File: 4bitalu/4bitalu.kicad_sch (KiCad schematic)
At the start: 34 parts, among them J1 Power, SW1 Opcode, SW2 Input Value, U1 74LS153 - 0, U2 74LS153 - 1, U3 74LS175, U4 74LS283, U5 74LS00 Stage0-1, U6 74LS00 Stage0-2, U7 74LS00 - Stage1

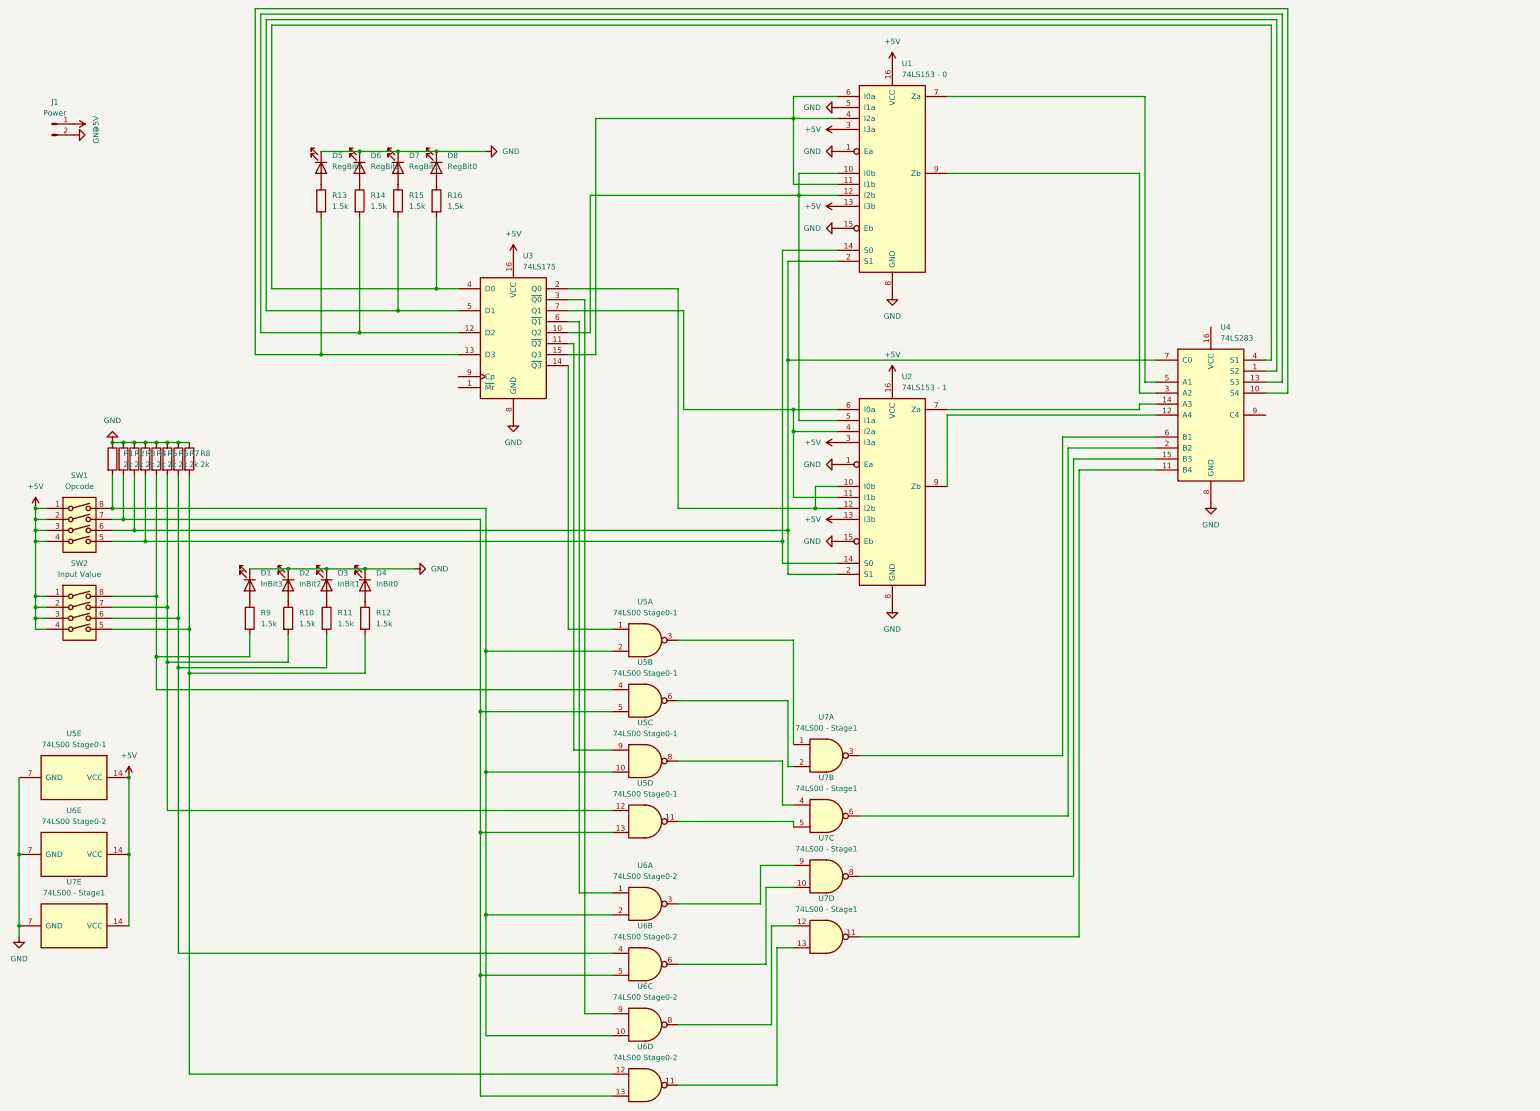
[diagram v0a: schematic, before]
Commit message: Rev 2 of PCB design
Known issues:

 * Pulldown resistors are too high (should be 1k)
 * Missing capacitors for power inputs on chips
 * Inputs on unused NAND gates are not tied high
 * Clock switch is in unexepected orientation
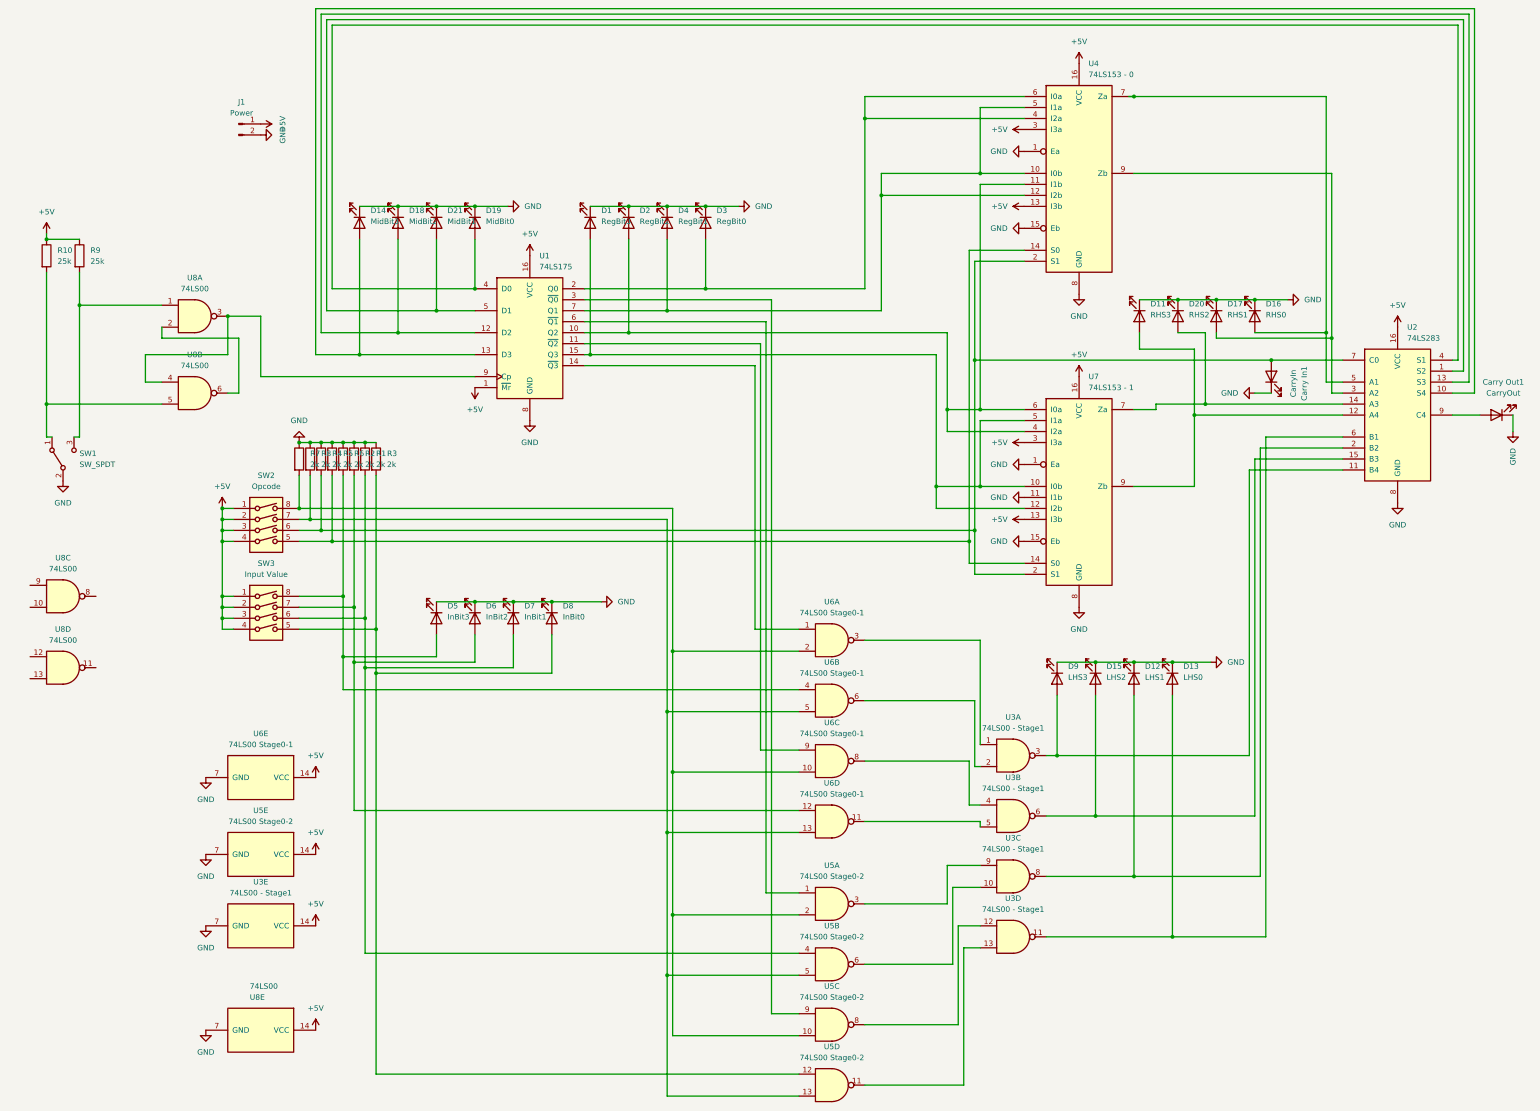
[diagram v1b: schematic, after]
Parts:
- removed R11, R12, R13, R14, R15, R16: 1.5k, Resistor_THT:R_Axial_DIN0204_L3.6mm_D1.6mm_P5.08mm_Horizontal, symbol Device:R
- added Carry In1: CarryIn, LED_THT:LED_D3.0mm, symbol Device:LED
- added Carry Out1: CarryOut, LED_THT:LED_D3.0mm, symbol Device:LED
- added D1: RegBit3, LED_THT:LED_D3.0mm, symbol Device:LED
- added D11: RHS3, LED_THT:LED_D3.0mm, symbol Device:LED
- added D12: LHS1, LED_THT:LED_D3.0mm, symbol Device:LED
- added D13: LHS0, LED_THT:LED_D3.0mm, symbol Device:LED
- added D15: LHS2, LED_THT:LED_D3.0mm, symbol Device:LED
- added D16: RHS0, LED_THT:LED_D3.0mm, symbol Device:LED
- added D17: RHS1, LED_THT:LED_D3.0mm, symbol Device:LED
- added D2: RegBit2, LED_THT:LED_D3.0mm, symbol Device:LED
- added D20: RHS2, LED_THT:LED_D3.0mm, symbol Device:LED
- added D3: RegBit0, LED_THT:LED_D3.0mm, symbol Device:LED
- added D4: RegBit1, LED_THT:LED_D3.0mm, symbol Device:LED
- added D9: LHS3, LED_THT:LED_D3.0mm, symbol Device:LED
- added SW1: SW_SPDT, Button_Switch_THT:SW_Slide_1P2T_CK_OS102011MS2Q, symbol Switch:SW_SPDT
- added U8: 74LS00, Package_DIP:DIP-14_W7.62mm, symbol 74xx:74LS00
- D14: renamed from D5; value RegBit3 -> MidBit3
- D18: renamed from D6; value RegBit2 -> MidBit2
- D19: renamed from D8; value RegBit0 -> MidBit0
- D21: renamed from D7; value RegBit1 -> MidBit1
- J1: footprint Connector_PinHeader_1.00mm:PinHeader_1x02_P1.00mm_Vertical -> Connector_PinHeader_2.54mm:PinHeader_1x02_P2.54mm_Vertical
- R1: renamed from R7; footprint Resistor_THT:R_Axial_DIN0204_L3.6mm_D1.6mm_P5.08mm_Horizontal -> Resistor_THT:R_Axial_DIN0207_L6.3mm_D2.5mm_P10.16mm_Horizontal
- R10, R9: value 1.5k -> 25k; footprint Resistor_THT:R_Axial_DIN0204_L3.6mm_D1.6mm_P5.08mm_Horizontal -> Resistor_THT:R_Axial_DIN0207_L6.3mm_D2.5mm_P10.16mm_Horizontal
- R2: renamed from R6; footprint Resistor_THT:R_Axial_DIN0204_L3.6mm_D1.6mm_P5.08mm_Horizontal -> Resistor_THT:R_Axial_DIN0207_L6.3mm_D2.5mm_P10.16mm_Horizontal
- R3: renamed from R8; footprint Resistor_THT:R_Axial_DIN0204_L3.6mm_D1.6mm_P5.08mm_Horizontal -> Resistor_THT:R_Axial_DIN0207_L6.3mm_D2.5mm_P10.16mm_Horizontal
- R4: renamed from R3; footprint Resistor_THT:R_Axial_DIN0204_L3.6mm_D1.6mm_P5.08mm_Horizontal -> Resistor_THT:R_Axial_DIN0207_L6.3mm_D2.5mm_P10.16mm_Horizontal
- R5: renamed from R4; footprint Resistor_THT:R_Axial_DIN0204_L3.6mm_D1.6mm_P5.08mm_Horizontal -> Resistor_THT:R_Axial_DIN0207_L6.3mm_D2.5mm_P10.16mm_Horizontal
- R6: renamed from R5; footprint Resistor_THT:R_Axial_DIN0204_L3.6mm_D1.6mm_P5.08mm_Horizontal -> Resistor_THT:R_Axial_DIN0207_L6.3mm_D2.5mm_P10.16mm_Horizontal
- R7: renamed from R1; footprint Resistor_THT:R_Axial_DIN0204_L3.6mm_D1.6mm_P5.08mm_Horizontal -> Resistor_THT:R_Axial_DIN0207_L6.3mm_D2.5mm_P10.16mm_Horizontal
- R8: renamed from R2; footprint Resistor_THT:R_Axial_DIN0204_L3.6mm_D1.6mm_P5.08mm_Horizontal -> Resistor_THT:R_Axial_DIN0207_L6.3mm_D2.5mm_P10.16mm_Horizontal
- renumbered D1 to D5, D2 to D6, D3 to D7, D4 to D8, SW1 to SW2, SW2 to SW3, U3 to U1, U4 to U2, U7 to U3, U1 to U4, U6 to U5, U5 to U6, U2 to U7
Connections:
- net +5V: now also R10.1, R9.1, U1.1 (~{Mr}), U2.16 (VCC), U8.14 (VCC)
- net GND: now also U7.11 (I1b), Carry In1.1 (K), Carry Out1.1 (K), D1.1 (K), D11.1 (K), D12.1 (K), D13.1 (K), D15.1 (K), D16.1 (K), D17.1 (K), D2.1 (K), D20.1 (K), D3.1 (K), D4.1 (K), D9.1 (K), SW1.2 (B), U8.7 (GND); no longer U4.5 (I1a)
- net at R1.2, SW3.6, U5.4: now also D7.2 (A)
- net at U4.10 (I0b), U4.12 (I2b): now also U1.7 (Q1), U4.5 (I1a), D4.2 (A); no longer U1.10 (Q2), U7.5 (I1a)
- net at U1.12 (D2), U2.13 (S3): now also D18.2 (A)
- net at U1.13 (D3), U2.10 (S4): now also D14.2 (A)
- net at U4.4 (I2a), U4.6 (I0a): now also U1.2 (Q0), D3.2 (A); no longer U1.15 (Q3), U4.11 (I1b)
- net at U7.10 (I0b), U7.12 (I2b): now also U1.15 (Q3), U7.5 (I1a), D1.2 (A); no longer U1.2 (Q0)
- net at U1.4 (D0), U2.4 (S1): now also D19.2 (A)
- net at U1.5 (D1), U2.1 (S2): now also D21.2 (A)
- net at U7.4 (I2a), U7.6 (I0a): now also U1.10 (Q2), U4.11 (I1b), D2.2 (A); no longer U1.7 (Q1), U7.11 (I1b)
- net at U1.9 (Cp): now also U8.3, U8.4
- net at U2.6 (B1): now also U3.11, D13.2 (A); no longer U3.3
- net at U2.11 (B4): now also U3.3, D9.2 (A); no longer U3.11
- net at U2.12 (A4), U7.9 (Zb): now also D11.2 (A)
- net at U2.14 (A3), U7.7 (Za): now also D20.2 (A)
- net at U2.15 (B3): now also U3.6, D15.2 (A); no longer U3.8
- net at U2.2 (B2): now also U3.8, D12.2 (A); no longer U3.6
- net at U2.3 (A2), U4.9 (Zb): now also D17.2 (A)
- net at U2.5 (A1), U4.7 (Za): now also D16.2 (A)
- net at R4.2, SW2.6, U2.7 (C0)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: now also Carry In1.2 (A)
- net at U2.9 (C4): now also Carry Out1.2 (A)
- net at R3.2, SW3.5, U5.12: now also D8.2 (A)
- net at R2.2, SW3.7, U6.12: now also D6.2 (A); no longer R10.2
- net at R6.2, SW3.8, U6.4: now also D5.2 (A); no longer R9.2
- new net: R9.2, SW1.3 (C), U8.1
- new net: U8.2, U8.6
- new net: R10.2, SW1.1 (A), U8.5
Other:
- moved on the sheet: D14, D18, D19, D21, D5, D6, D7, D8, J1, R1, R2, R3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

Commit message: Revision 3 mostly ready
 * Adds caps on power
 * Inverts logic for clock switch
 * Adds optional clock LED
 * Changes pulldown resistors to 1k

Note: this design should also work with 3.3v logic and LEDs
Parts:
- added C1, C2, C3, C4, C5, C6, C7, C8: .1uf, Capacitor_THT:C_Disc_D3.0mm_W1.6mm_P2.50mm, symbol Device:C
- added ClockState1: ClockState, LED_THT:LED_D3.0mm, symbol Device:LED
- R1: renamed from R3; value 2k -> 1k
- R2: renamed from R1; value 2k -> 1k
- R3: renamed from R2; value 2k -> 1k
- R4: renamed from R6; value 2k -> 1k
- R5: value 2k -> 1k
- R6: renamed from R4; value 2k -> 1k
- R7: renamed from R8; value 2k -> 1k
- R8: renamed from R7; value 2k -> 1k
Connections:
- net +5V: now also U8.10, U8.12, U8.13, U8.9, C1.1, C2.1, C3.1, C4.1, C5.1, C6.1, C7.1, C8.1
- net GND: now also C1.2, C2.2, C3.2, C4.2, C5.2, C6.2, C7.2, C8.2, ClockState1.1 (K)
- net at U8.3, U8.4: no longer U1.9 (Cp)
- net at U8.2, U8.6: now also U1.9 (Cp), ClockState1.2 (A)
